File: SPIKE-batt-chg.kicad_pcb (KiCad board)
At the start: 2 copper layers, 174.5 x 30 mm, 109 parts, among them IC1 CH224K, IC2 CN3702, IC3 CN3702, IC4 CN3702, J1 USB_C_Receptacle_USB2.0, J2 Barrel_Jack_Switch, J3 Conn_01x03_Pin, J4 Conn_01x03_Pin, J5 Conn_01x03_Pin, Q1 PMOS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

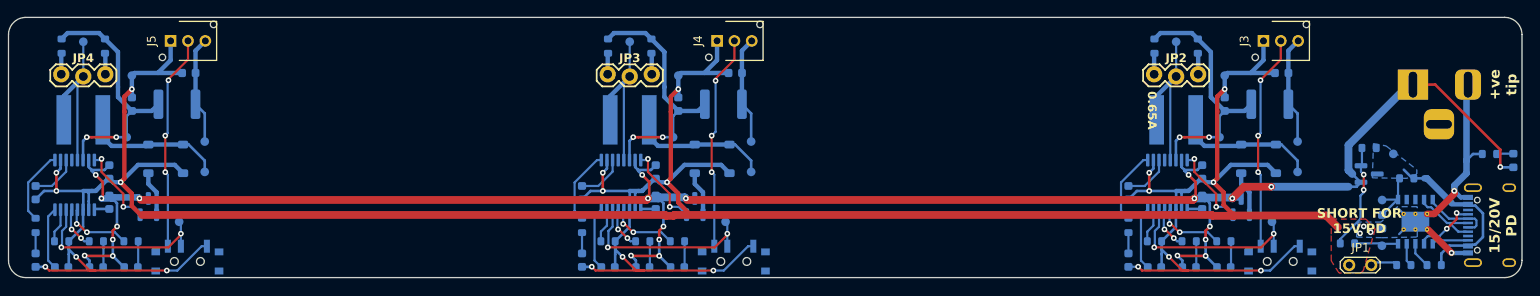
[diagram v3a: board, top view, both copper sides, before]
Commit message: Added fuse and shunt diode
For reverse polarity protection
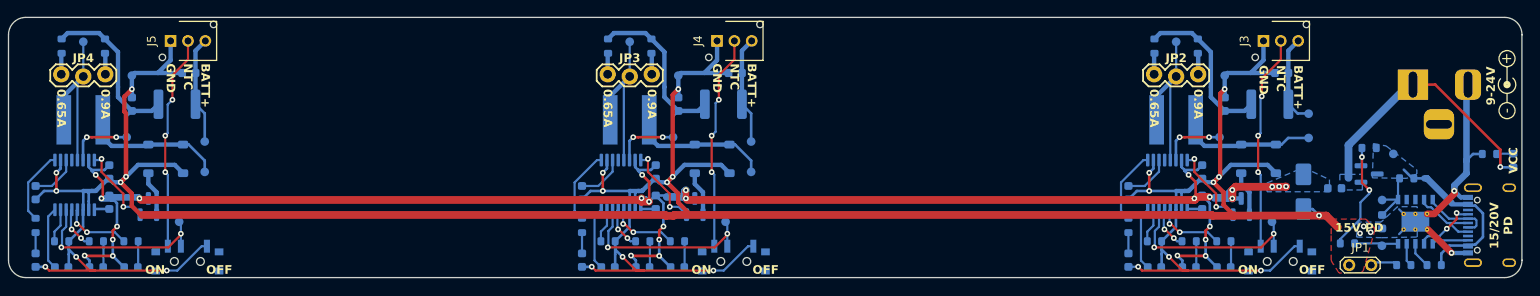
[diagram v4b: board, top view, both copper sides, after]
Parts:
- added D14: D_Schottky, Diode_SMD:D_SMA, B.Cu at (241.8, 142.6)
- added F4: 3A Fuse, Fuse:Fuse_0603_1608Metric, B.Cu at (245.4, 142.2)
- added REF**: Symbol_Barrel_Polarity, Symbol:Symbol_Barrel_Polarity, F.Cu at (265.2, 130.2)
- moved TP6 4.11 mm to (242.4, 136.4)
- moved TP7 3.46 mm to (242.4, 133.6)
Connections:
- C10 pad 1: VCC -> /CN3702 Charger1/VCC
- C16 pad 1: VCC -> /CN3702 Charger1/VCC
- C17 pad 1: VCC -> /CN3702 Charger1/VCC
- C2 pad 1: VCC -> /CN3702 Charger1/VCC
- C3 pad 1: VCC -> /CN3702 Charger1/VCC
- C9 pad 1: VCC -> /CN3702 Charger1/VCC
- D10 pad 2: VCC -> /CN3702 Charger1/VCC
- D11 pad 2: VCC -> /CN3702 Charger1/VCC
- D2 pad 2: VCC -> /CN3702 Charger1/VCC
- D3 pad 2: VCC -> /CN3702 Charger1/VCC
- D6 pad 2: VCC -> /CN3702 Charger1/VCC
- D7 pad 2: VCC -> /CN3702 Charger1/VCC
- IC2 pad 15: VCC -> /CN3702 Charger1/VCC
- IC3 pad 15: VCC -> /CN3702 Charger1/VCC
- IC4 pad 15: VCC -> /CN3702 Charger1/VCC
- Q2 pad 3: VCC -> /CN3702 Charger1/VCC
- Q3 pad 3: VCC -> /CN3702 Charger1/VCC
- Q4 pad 3: VCC -> /CN3702 Charger1/VCC
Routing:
- net VCC: track 247.9 -> 30.8 mm, vias 23 -> 1
- net /CN3702 Charger1/VCC: track 0.00 -> 213.7 mm, vias 0 -> 28
- net Net-(Q1-G): track 12.3 -> 14.7 mm
- net GND: track 325.4 -> 327.7 mm, vias 11 -> 15
- net /CN3702 Charger1/+BATT: track 20.3 -> 18.3 mm
- added copper zone on B.Cu, net /CN3702 Charger1/VCC
- added copper zone on B.Cu, net VCC
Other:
- board text added: "+"
- board text added: "-"
- board text added: "0.9A"
- board text added: "15V PD"
- board text added: "9-24V"
- board text added: "BATT+"
- board text added: "GND"
- board text added: "NTC"
- board text added: "OFF"
- board text added: "ON"
- board text added: "VCC"
- board text removed: "+ve tip"
- board text removed: "SHORT FOR 15V PD"

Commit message: Added tooling and mounting holes
- Added pinout for "done" pin on charger for future use
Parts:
- added J6: Conn_01x01_Pin, Connector_PinHeader_2.54mm:PinHeader_1x01_P2.54mm_Vertical, F.Cu at (217.0, 149.0)
- added J7: Conn_01x01_Pin, Connector_PinHeader_2.54mm:PinHeader_1x01_P2.54mm_Vertical, F.Cu at (154.0, 149.2)
- added J8: Conn_01x01_Pin, Connector_PinHeader_2.54mm:PinHeader_1x01_P2.54mm_Vertical, F.Cu at (94.8, 137.0)
- added REF**: MountingHole_3.2mm_M3_ISO7380, MountingHole:MountingHole_3.2mm_M3_ISO7380, F.Cu at (125.0, 132.5)
- added REF**: MountingHole_2.1mm, MountingHole:MountingHole_2.1mm, F.Cu at (94.2, 124.5)
- added REF**: MountingHole_2.1mm, MountingHole:MountingHole_2.1mm, F.Cu at (264.2, 124.0)
- added REF**: MountingHole_3.2mm_M3_ISO7380, MountingHole:MountingHole_3.2mm_M3_ISO7380, F.Cu at (215.0, 132.5)
- added REF**: MountingHole_3.2mm_M3_ISO7380, MountingHole:MountingHole_3.2mm_M3_ISO7380, F.Cu at (187.5, 132.5)
- added REF**: MountingHole_3.2mm_M3_ISO7380, MountingHole:MountingHole_3.2mm_M3_ISO7380, F.Cu at (125.0, 149.2)
- added REF**: MountingHole_3.2mm_M3_ISO7380, MountingHole:MountingHole_3.2mm_M3_ISO7380, F.Cu at (187.5, 149.2)
- added REF**: MountingHole_2.1mm, MountingHole:MountingHole_2.1mm, F.Cu at (194.5, 151.0)
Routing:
- net Net-(IC4-DONE): track 4.93 -> 16.9 mm
- net Net-(IC3-DONE): track 4.93 -> 14.6 mm
- net Net-(IC2-DONE): track 4.93 -> 14.6 mm
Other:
- board text added: "JLCJLCJLCJLC"

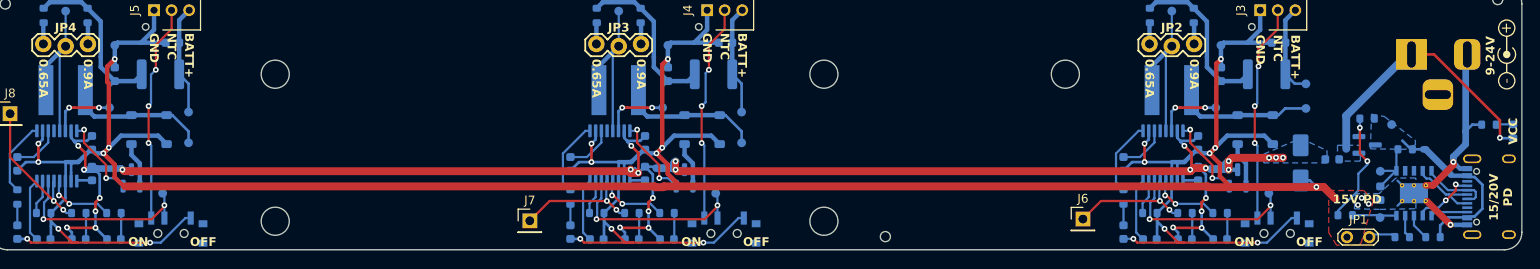
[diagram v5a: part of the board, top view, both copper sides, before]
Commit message: Change grid origin, generate production files
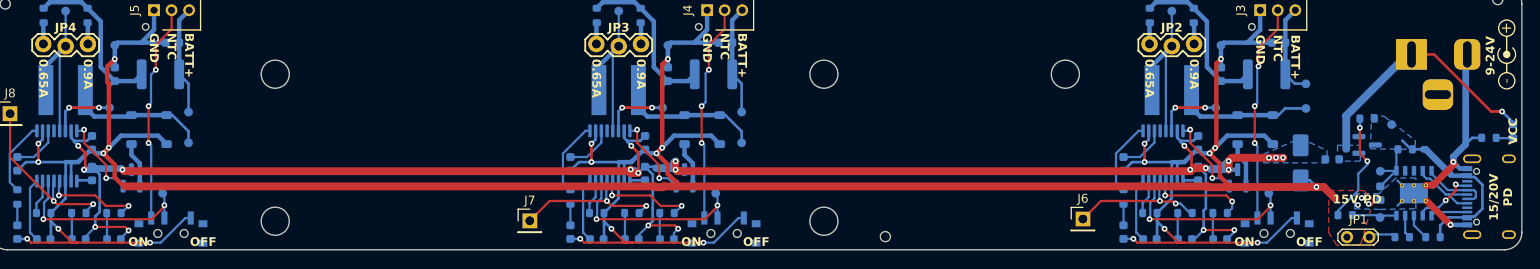
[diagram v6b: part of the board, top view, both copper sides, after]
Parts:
- moved R4 1.50 mm to (263.2, 139.8)
- turned D1 to 90 degrees
- turned D10 to 0 degrees
- turned D11 to 0 degrees
- turned D2 to 0 degrees
- turned D3 to 0 degrees
- turned D6 to 0 degrees
- turned D7 to 0 degrees
- turned R13 to 0 degrees
- turned R14 to 0 degrees
- turned R19 to 0 degrees
- turned R20 to 0 degrees
- turned R7 to 0 degrees
- turned R8 to 0 degrees
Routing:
- net Net-(IC4-DONE): track 16.9 -> 20.3 mm
- net Net-(IC4-CHRG): track 7.94 -> 11.3 mm
- net Net-(IC3-CHRG): track 7.94 -> 11.3 mm
- net Net-(IC3-DONE): track 14.6 -> 17.9 mm
- net Net-(IC2-CHRG): track 7.94 -> 11.1 mm
- net Net-(IC2-DONE): track 14.6 -> 16.3 mm
- net VCC: track 30.8 -> 29.1 mm
- net /CN3702 Charger1/VCC: track 213.7 -> 214.5 mm, vias 28 -> 22

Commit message: Fixed problems after PCB fab
- SOT23 MOSFET footprint does not match part, needs to rotate (rerouting
  not done yet)

- EOC Resistor set to 100k
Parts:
- R15, R21, R9: value 0R -> 100k
- turned Q1 to -90 degrees
- turned Q2 to 0 degrees
- turned Q3 to 0 degrees
- turned Q4 to 0 degrees
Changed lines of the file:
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@@
   )
   (footprint "Package_TO_SOT_SMD:SOT-23" (layer "B.Cu")
-    (at 171.625 144.312184 90)
+    (at 171.625 144.312184)
     (descr "SOT, 3 Pin (https://www.jedec.org/system/files/docs/to-236h.pdf variant AB), generated with kicad-footprint-generator ipc_gullwing_generator.py")
     (tags "SOT TO_SOT_SMD")
@@
     (property "ki_keywords" "transistor PMOS P-MOS P-MOSFET simulation")
     (attr smd)
-    (fp_text reference "Q3" (at 2.5 0 unlocked) (layer "B.SilkS")
+    (fp_text reference "Q3" (at 2.5 0 -90 unlocked) (layer "B.SilkS")
         (effects (font (size 1 1) (thickness 0.2)) (justify mirror))
     )
-    (fp_text value "PMOS" (at 0 -2.4 90) (layer "B.Fab")
+    (fp_text value "PMOS" (at 0 -2.4) (layer "B.Fab")
         (effects (font (size 1 1) (thickness 0.15)) (justify mirror))
     )
-    (fp_text user "${REFERENCE}" (at 0 0 90) (layer "B.Fab")
+    (fp_text user "${REFERENCE}" (at 0 0) (layer "B.Fab")
         (effects (font (size 0.32 0.32) (thickness 0.05)) (justify mirror))
     )
@@
     (fp_line (start 0.65 1.45) (end 0.65 -1.45)
       (stroke (width 0.1) (type solid)) (layer "B.Fab"))
-    (pad "1" smd roundrect (at -0.9375 0.95 90) (size 1.475 0.6) (layers "B.Cu" "B.Paste" "B.Mask") (roundrect_rratio 0.25)
+    (pad "1" smd roundrect (at 0.9375 0) (size 1.475 0.6) (layers "B.Cu" "B.Paste" "B.Mask") (roundrect_rratio 0.25)
       (net 24 "Net-(D8-A)") (pinfunction "D") (pintype "passive"))
-    (pad "2" smd roundrect (at -0.9375 -0.95 90) (size 1.475 0.6) (layers "B.Cu" "B.Paste" "B.Mask") (roundrect_rratio 0.25)
+    (pad "2" smd roundrect (at -0.9375 0.95) (size 1.475 0.6) (layers "B.Cu" "B.Paste" "B.Mask") (roundrect_rratio 0.25)
       (net 55 "Net-(IC3-DRV)") (pinfunction "G") (pintype "input"))
-    (pad "3" smd roundrect (at 0.9375 0 90) (size 1.475 0.6) (layers "B.Cu" "B.Paste" "B.Mask") (roundrect_rratio 0.25)
+    (pad "3" smd roundrect (at -0.9375 -0.95) (size 1.475 0.6) (layers "B.Cu" "B.Paste" "B.Mask") (roundrect_rratio 0.25)
       (net 87 "/CN3702 Charger1/VCC") (pinfunction "S") (pintype "passive"))
     (model "${KICAD6_3DMODEL_DIR}/Package_TO_SOT_SMD.3dshapes/SOT-23.wrl"
@@
   )
   (footprint "Package_TO_SOT_SMD:SOT-23" (layer "B.Cu")
-    (at 249.373036 140.556984)
+    (at 249.373036 140.556984 -90)
     (descr "SOT, 3 Pin (https://www.jedec.org/system/files/docs/to-236h.pdf variant AB), generated with kicad-footprint-generator ipc_gullwing_generator.py")
     (tags "SOT TO_SOT_SMD")
@@
     (property "ki_keywords" "transistor PMOS P-MOS P-MOSFET simulation")
     (attr smd)
-    (fp_text reference "Q1" (at -2.5 0 90 unlocked) (layer "B.SilkS")
+    (fp_text reference "Q1" (at -2.5 0 unlocked) (layer "B.SilkS")
         (effects (font (size 1 1) (thickness 0.2)) (justify mirror))
     )
-    (fp_text value "PMOS" (at 0 -2.4) (layer "B.Fab")
+    (fp_text value "PMOS" (at 0 -2.4 90) (layer "B.Fab")
         (effects (font (size 1 1) (thickness 0.15)) (justify mirror))
     )
-    (fp_text user "${REFERENCE}" (at 0 0) (layer "B.Fab")
+    (fp_text user "${REFERENCE}" (at 0 0 90) (layer "B.Fab")
         (effects (font (size 0.32 0.32) (thickness 0.05)) (justify mirror))
     )
@@
     (fp_line (start 0.65 1.45) (end 0.65 -1.45)
       (stroke (width 0.1) (type solid)) (layer "B.Fab"))
-    (pad "1" smd roundrect (at -0.9375 0.95) (size 1.475 0.6) (layers "B.Cu" "B.Paste" "B.Mask") (roundrect_rratio 0.25)
+    (pad "1" smd roundrect (at 0.9375 0 270) (size 1.475 0.6) (layers "B.Cu" "B.Paste" "B.Mask") (roundrect_rratio 0.25)
       (net 3 "VCC") (pinfunction "D") (pintype "passive"))
-    (pad "2" smd roundrect (at -0.9375 -0.95) (size 1.475 0.6) (layers "B.Cu" "B.Paste" "B.Mask") (roundrect_rratio 0.25)
+    (pad "2" smd roundrect (at -0.9375 0.95 270) (size 1.475 0.6) (layers "B.Cu" "B.Paste" "B.Mask") (roundrect_rratio 0.25)
       (net 80 "Net-(Q1-G)") (pinfunction "G") (pintype "input"))
-    (pad "3" smd roundrect (at 0.9375 0) (size 1.475 0.6) (layers "B.Cu" "B.Paste" "B.Mask") (roundrect_rratio 0.25)
+    (pad "3" smd roundrect (at -0.9375 -0.95 270) (size 1.475 0.6) (layers "B.Cu" "B.Paste" "B.Mask") (roundrect_rratio 0.25)
       (net 65 "VBUS") (pinfunction "S") (pintype "passive"))
     (model "${KICAD6_3DMODEL_DIR}/Package_TO_SOT_SMD.3dshapes/SOT-23.wrl"
@@
   )
   (footprint "Package_TO_SOT_SMD:SOT-23" (layer "B.Cu")
-    (at 234.625 144.312184 90)
+    (at 234.625 144.312184)
     (descr "SOT, 3 Pin (https://www.jedec.org/system/files/docs/to-236h.pdf variant AB), generated with kicad-footprint-generator ipc_gullwing_generator.py")
     (tags "SOT TO_SOT_SMD")
@@
     (property "ki_keywords" "transistor PMOS P-MOS P-MOSFET simulation")
     (attr smd)
-    (fp_text reference "Q2" (at 2.5 0 unlocked) (layer "B.SilkS")
+    (fp_text reference "Q2" (at 2.5 0 -90 unlocked) (layer "B.SilkS")
         (effects (font (size 1 1) (thickness 0.2)) (justify mirror))
     )
-    (fp_text value "PMOS" (at 0 -2.4 90) (layer "B.Fab")
+    (fp_text value "PMOS" (at 0 -2.4) (layer "B.Fab")
         (effects (font (size 1 1) (thickness 0.15)) (justify mirror))
     )
-    (fp_text user "${REFERENCE}" (at 0 0 90) (layer "B.Fab")
+    (fp_text user "${REFERENCE}" (at 0 0) (layer "B.Fab")
         (effects (font (size 0.32 0.32) (thickness 0.05)) (justify mirror))
     )
@@
     (fp_line (start 0.65 1.45) (end 0.65 -1.45)
       (stroke (width 0.1) (type solid)) (layer "B.Fab"))
-    (pad "1" smd roundrect (at -0.9375 0.95 90) (size 1.475 0.6) (layers "B.Cu" "B.Paste" "B.Mask") (roundrect_rratio 0.25)
+    (pad "1" smd roundrect (at 0.9375 0) (size 1.475 0.6) (layers "B.Cu" "B.Paste" "B.Mask") (roundrect_rratio 0.25)
       (net 20 "Net-(D4-A)") (pinfunction "D") (pintype "passive"))
-    (pad "2" smd roundrect (at -0.9375 -0.95 90) (size 1.475 0.6) (layers "B.Cu" "B.Paste" "B.Mask") (roundrect_rratio 0.25)
+    (pad "2" smd roundrect (at -0.9375 0.95) (size 1.475 0.6) (layers "B.Cu" "B.Paste" "B.Mask") (roundrect_rratio 0.25)
       (net 44 "Net-(IC2-DRV)") (pinfunction "G") (pintype "input"))
-    (pad "3" smd roundrect (at 0.9375 0 90) (size 1.475 0.6) (layers "B.Cu" "B.Paste" "B.Mask") (roundrect_rratio 0.25)
+    (pad "3" smd roundrect (at -0.9375 -0.95) (size 1.475 0.6) (layers "B.Cu" "B.Paste" "B.Mask") (roundrect_rratio 0.25)
       (net 87 "/CN3702 Charger1/VCC") (pinfunction "S") (pintype "passive"))
     (model "${KICAD6_3DMODEL_DIR}/Package_TO_SOT_SMD.3dshapes/SOT-23.wrl"
@@
   )
   (footprint "Package_TO_SOT_SMD:SOT-23" (layer "B.Cu")
-    (at 108.625 144.312184 90)
+    (at 108.625 144.312184)
     (descr "SOT, 3 Pin (https://www.jedec.org/system/files/docs/to-236h.pdf variant AB), generated with kicad-footprint-generator ipc_gullwing_generator.py")
     (tags "SOT TO_SOT_SMD")
@@
     (property "ki_keywords" "transistor PMOS P-MOS P-MOSFET simulation")
     (attr smd)
-    (fp_text reference "Q4" (at 2.5 0 unlocked) (layer "B.SilkS")
+    (fp_text reference "Q4" (at 2.5 0 -90 unlocked) (layer "B.SilkS")
         (effects (font (size 1 1) (thickness 0.2)) (justify mirror))
     )
-    (fp_text value "PMOS" (at 0 -2.4 90) (layer "B.Fab")
+    (fp_text value "PMOS" (at 0 -2.4) (layer "B.Fab")
         (effects (font (size 1 1) (thickness 0.15)) (justify mirror))
     )
-    (fp_text user "${REFERENCE}" (at 0 0 90) (layer "B.Fab")
+    (fp_text user "${REFERENCE}" (at 0 0) (layer "B.Fab")
         (effects (font (size 0.32 0.32) (thickness 0.05)) (justify mirror))
     )
@@
     (fp_line (start 0.65 1.45) (end 0.65 -1.45)
       (stroke (width 0.1) (type solid)) (layer "B.Fab"))
-    (pad "1" smd roundrect (at -0.9375 0.95 90) (size 1.475 0.6) (layers "B.Cu" "B.Paste" "B.Mask") (roundrect_rratio 0.25)
+    (pad "1" smd roundrect (at 0.9375 0) (size 1.475 0.6) (layers "B.Cu" "B.Paste" "B.Mask") (roundrect_rratio 0.25)
       (net 28 "Net-(D12-A)") (pinfunction "D") (pintype "passive"))
-    (pad "2" smd roundrect (at -0.9375 -0.95 90) (size 1.475 0.6) (layers "B.Cu" "B.Paste" "B.Mask") (roundrect_rratio 0.25)
+    (pad "2" smd roundrect (at -0.9375 0.95) (size 1.475 0.6) (layers "B.Cu" "B.Paste" "B.Mask") (roundrect_rratio 0.25)
       (net 64 "Net-(IC4-DRV)") (pinfunction "G") (pintype "input"))
-    (pad "3" smd roundrect (at 0.9375 0 90) (size 1.475 0.6) (layers "B.Cu" "B.Paste" "B.Mask") (roundrect_rratio 0.25)
+    (pad "3" smd roundrect (at -0.9375 -0.95) (size 1.475 0.6) (layers "B.Cu" "B.Paste" "B.Mask") (roundrect_rratio 0.25)
       (net 87 "/CN3702 Charger1/VCC") (pinfunction "S") (pintype "passive"))
     (model "${KICAD6_3DMODEL_DIR}/Package_TO_SOT_SMD.3dshapes/SOT-23.wrl"
@@
         (effects (font (size 1 1) (thickness 0.2)) (justify mirror))
     )
-    (fp_text value "0R" (at 0 -1.43) (layer "B.Fab")
+    (fp_text value "100k" (at 0 -1.43) (layer "B.Fab")
         (effects (font (size 1 1) (thickness 0.15)) (justify mirror))
     )
@@
         (effects (font (size 1 1) (thickness 0.2)) (justify mirror))
     )
-    (fp_text value "0R" (at 0 -1.43) (layer "B.Fab")
+    (fp_text value "100k" (at 0 -1.43) (layer "B.Fab")
         (effects (font (size 1 1) (thickness 0.15)) (justify mirror))
     )
@@
         (effects (font (size 1 1) (thickness 0.2)) (justify mirror))
     )
-    (fp_text value "0R" (at 0 -1.43) (layer "B.Fab")
+    (fp_text value "100k" (at 0 -1.43) (layer "B.Fab")
         (effects (font (size 1 1) (thickness 0.15)) (justify mirror))
     )
